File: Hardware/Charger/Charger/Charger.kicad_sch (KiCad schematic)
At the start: 0 parts

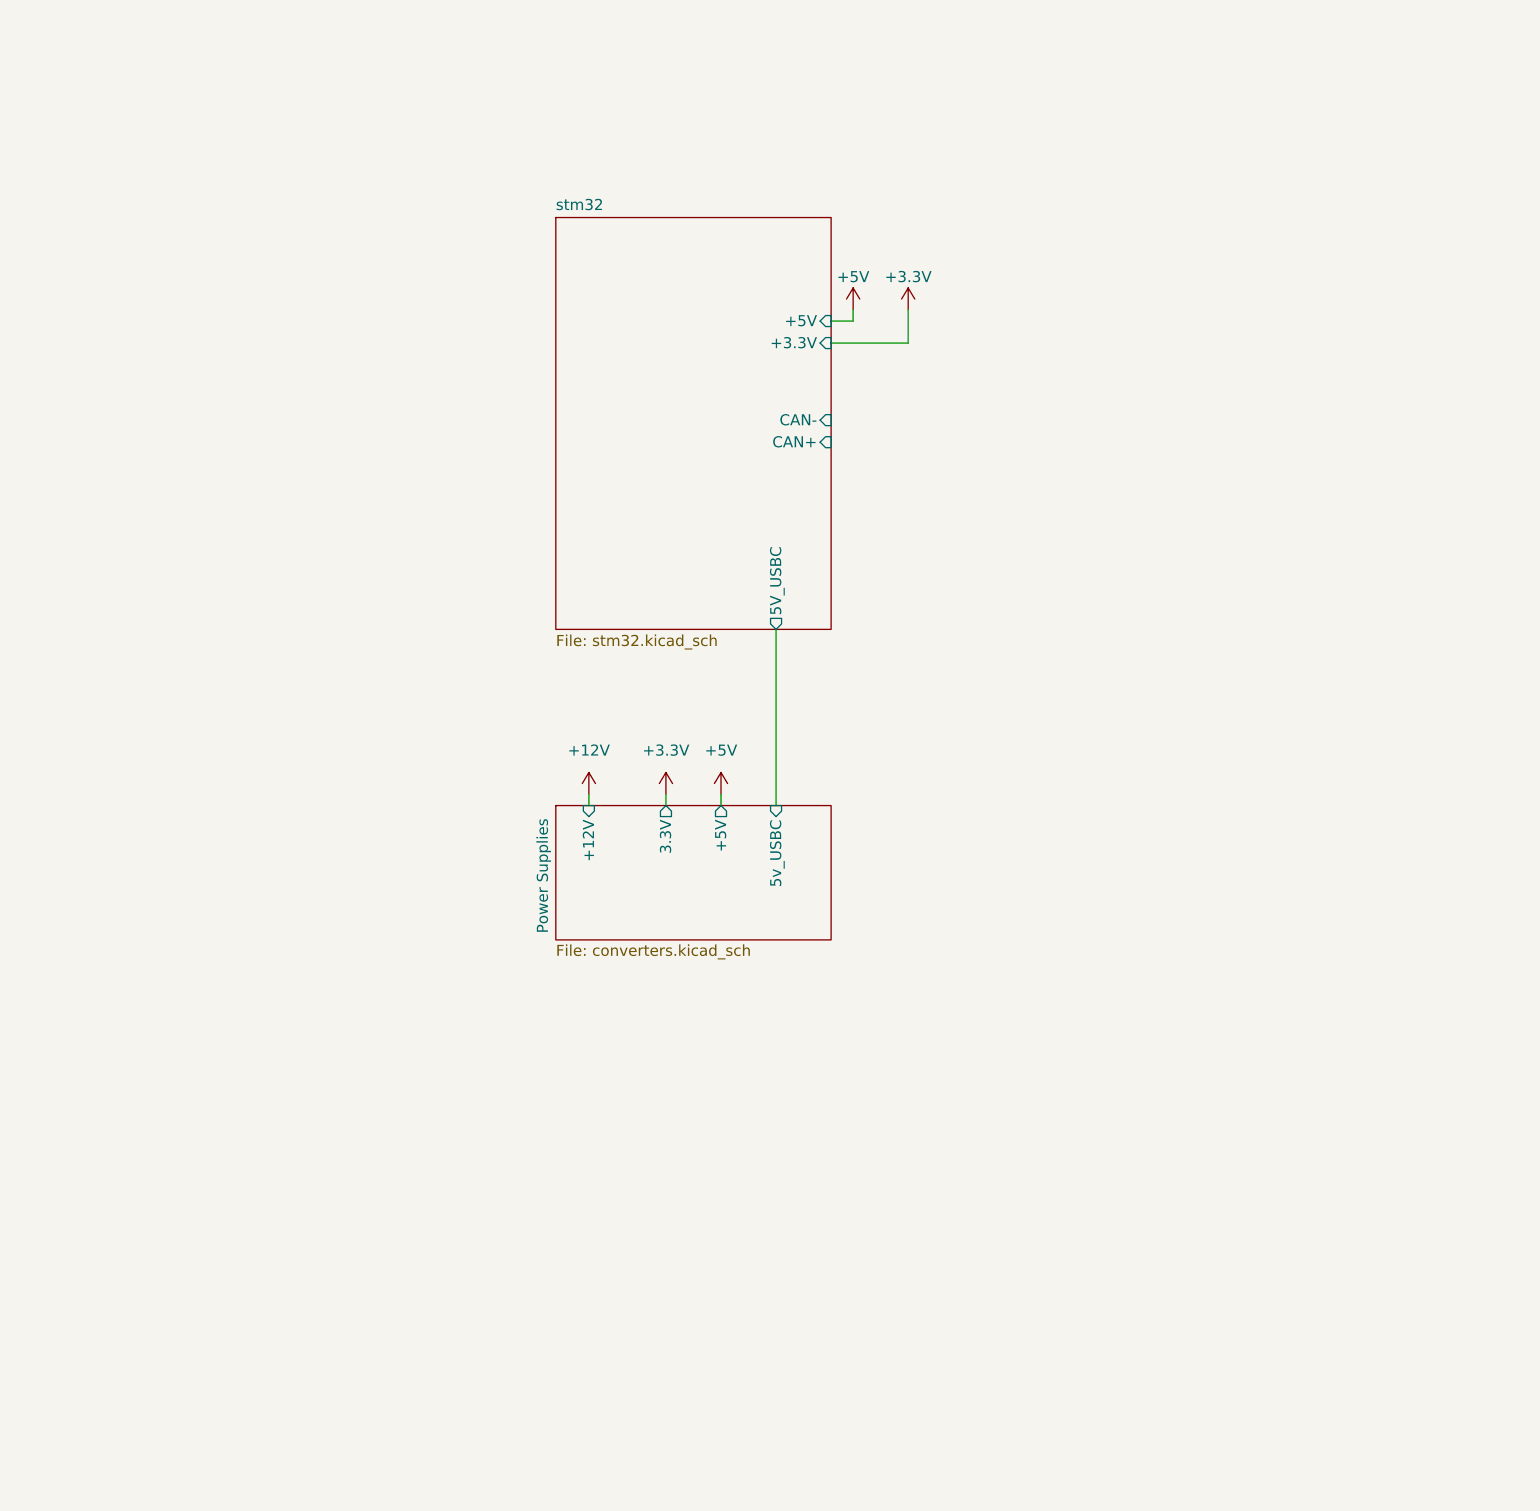
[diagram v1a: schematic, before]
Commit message: Added: Contactor control, Voltage sense, I2C comms for oled screen, 3v3 and 5v converters, power switch
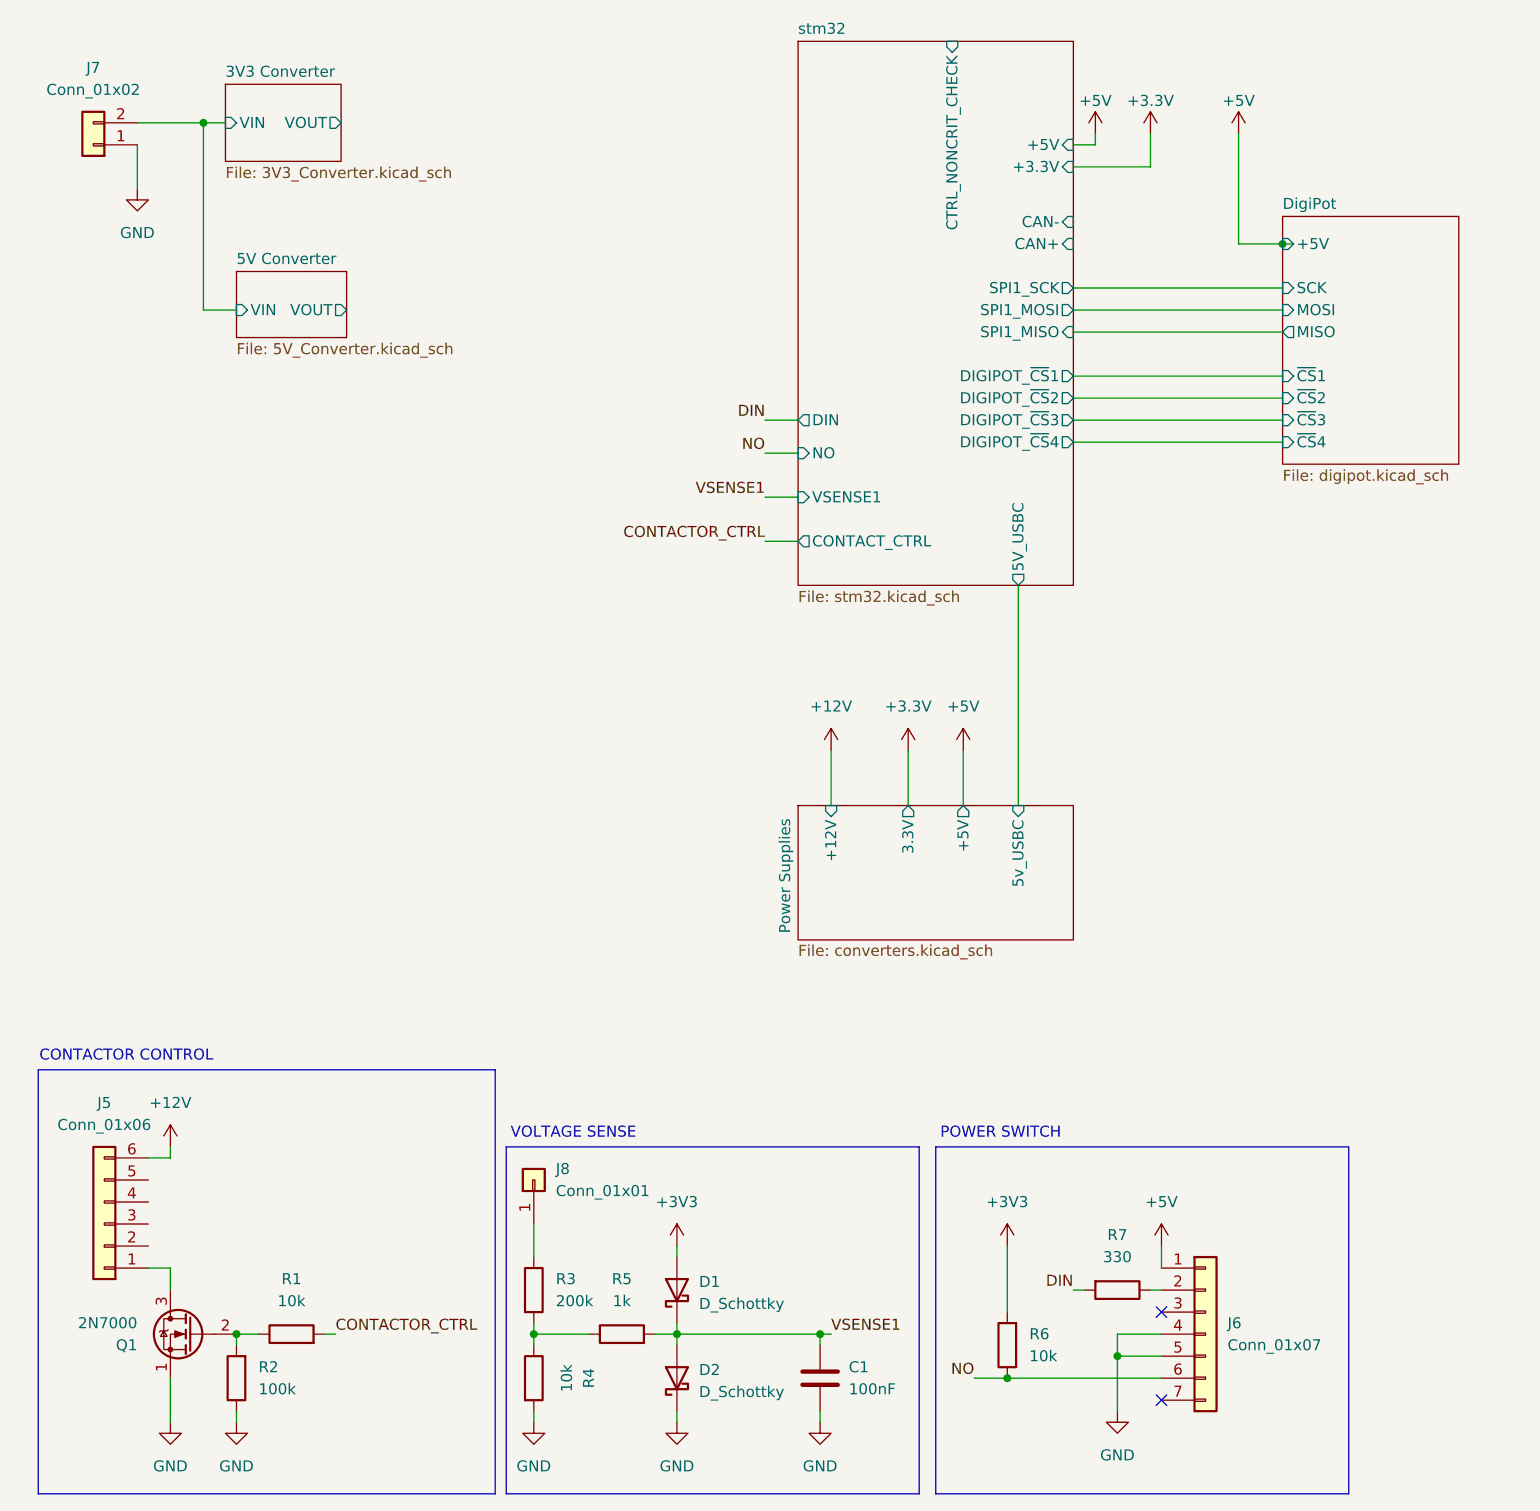
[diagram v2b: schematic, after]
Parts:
- added C1: 100nF, Capacitor_SMD:C_0603_1608Metric, symbol Device:C
- added D1, D2: D_Schottky, Diode_SMD:D_0201_0603Metric, symbol Device:D_Schottky
- added J5: Conn_01x06, Connector_Molex:Molex_Micro-Fit_3.0_43650-0600_1x06_P3.00mm_Horizontal, symbol Connector_Generic:Conn_01x06
- added J6: Conn_01x07, symbol Connector_Generic:Conn_01x07
- added J7: Conn_01x02, symbol Connector_Generic:Conn_01x02
- added J8: Conn_01x01, symbol Connector_Generic:Conn_01x01
- added Q1: 2N7000, Package_TO_SOT_THT:TO-92_Inline, symbol Transistor_FET:2N7000
- added R1, R4, R6: 10k, Resistor_SMD:R_0603_1608Metric, symbol Device:R
- added R2: 100k, Resistor_SMD:R_0603_1608Metric, symbol Device:R
- added R3: 200k, Resistor_SMD:R_0603_1608Metric, symbol Device:R
- added R5: 1k, Resistor_SMD:R_0603_1608Metric, symbol Device:R
- added R7: 330, Resistor_SMD:R_0603_1608Metric, symbol Device:R
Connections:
- net +12V: now also J5.6 (Pin_6)
- net +5V: now also J6.1 (Pin_1)
- new net: J8.1 (Pin_1), R3.1
- new net: R3.2, R4.1, R5.1
- new net: Q1.2 (G), R1.1, R2.2
- new net: J5.1 (Pin_1), Q1.3 (D)
- new net: J6.2 (Pin_2), R7.1
- new net +3V3: D1.2 (A), R6.2
- new net 3V3 Converter/VIN: J7.2 (Pin_2)
- new net CONTACTOR_CTRL: R1.2
- new net DIN: R7.2
- new net GND: C1.2, D2.1 (K), J6.4 (Pin_4), J6.5 (Pin_5), J7.1 (Pin_1), Q1.1 (S), R2.1, R4.2
- new net NO: J6.6 (Pin_6), R6.1
- new net VSENSE1: C1.1, D1.1 (K), D2.2 (A), R5.2
- no-connect marks 0 -> 2
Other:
- added sheet 3V3 Converter (3V3_Converter.kicad_sch)
- added sheet 5V Converter (5V_Converter.kicad_sch)
- added sheet DigiPot (digipot.kicad_sch)
- sheet stm32 ports: added CONTACT_CTRL, CTRL_NONCRIT_CHECK, DIGIPOT_~{CS}1, DIGIPOT_~{CS}2, DIGIPOT_~{CS}3, DIGIPOT_~{CS}4, DIN, NO, SPI1_MISO, SPI1_MOSI, SPI1_SCK, VSENSE1; removed none
- note added: "CONTACTOR CONTROL"
- note added: "POWER SWITCH"
- note added: "VOLTAGE SENSE"

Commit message: Few updates to connectors
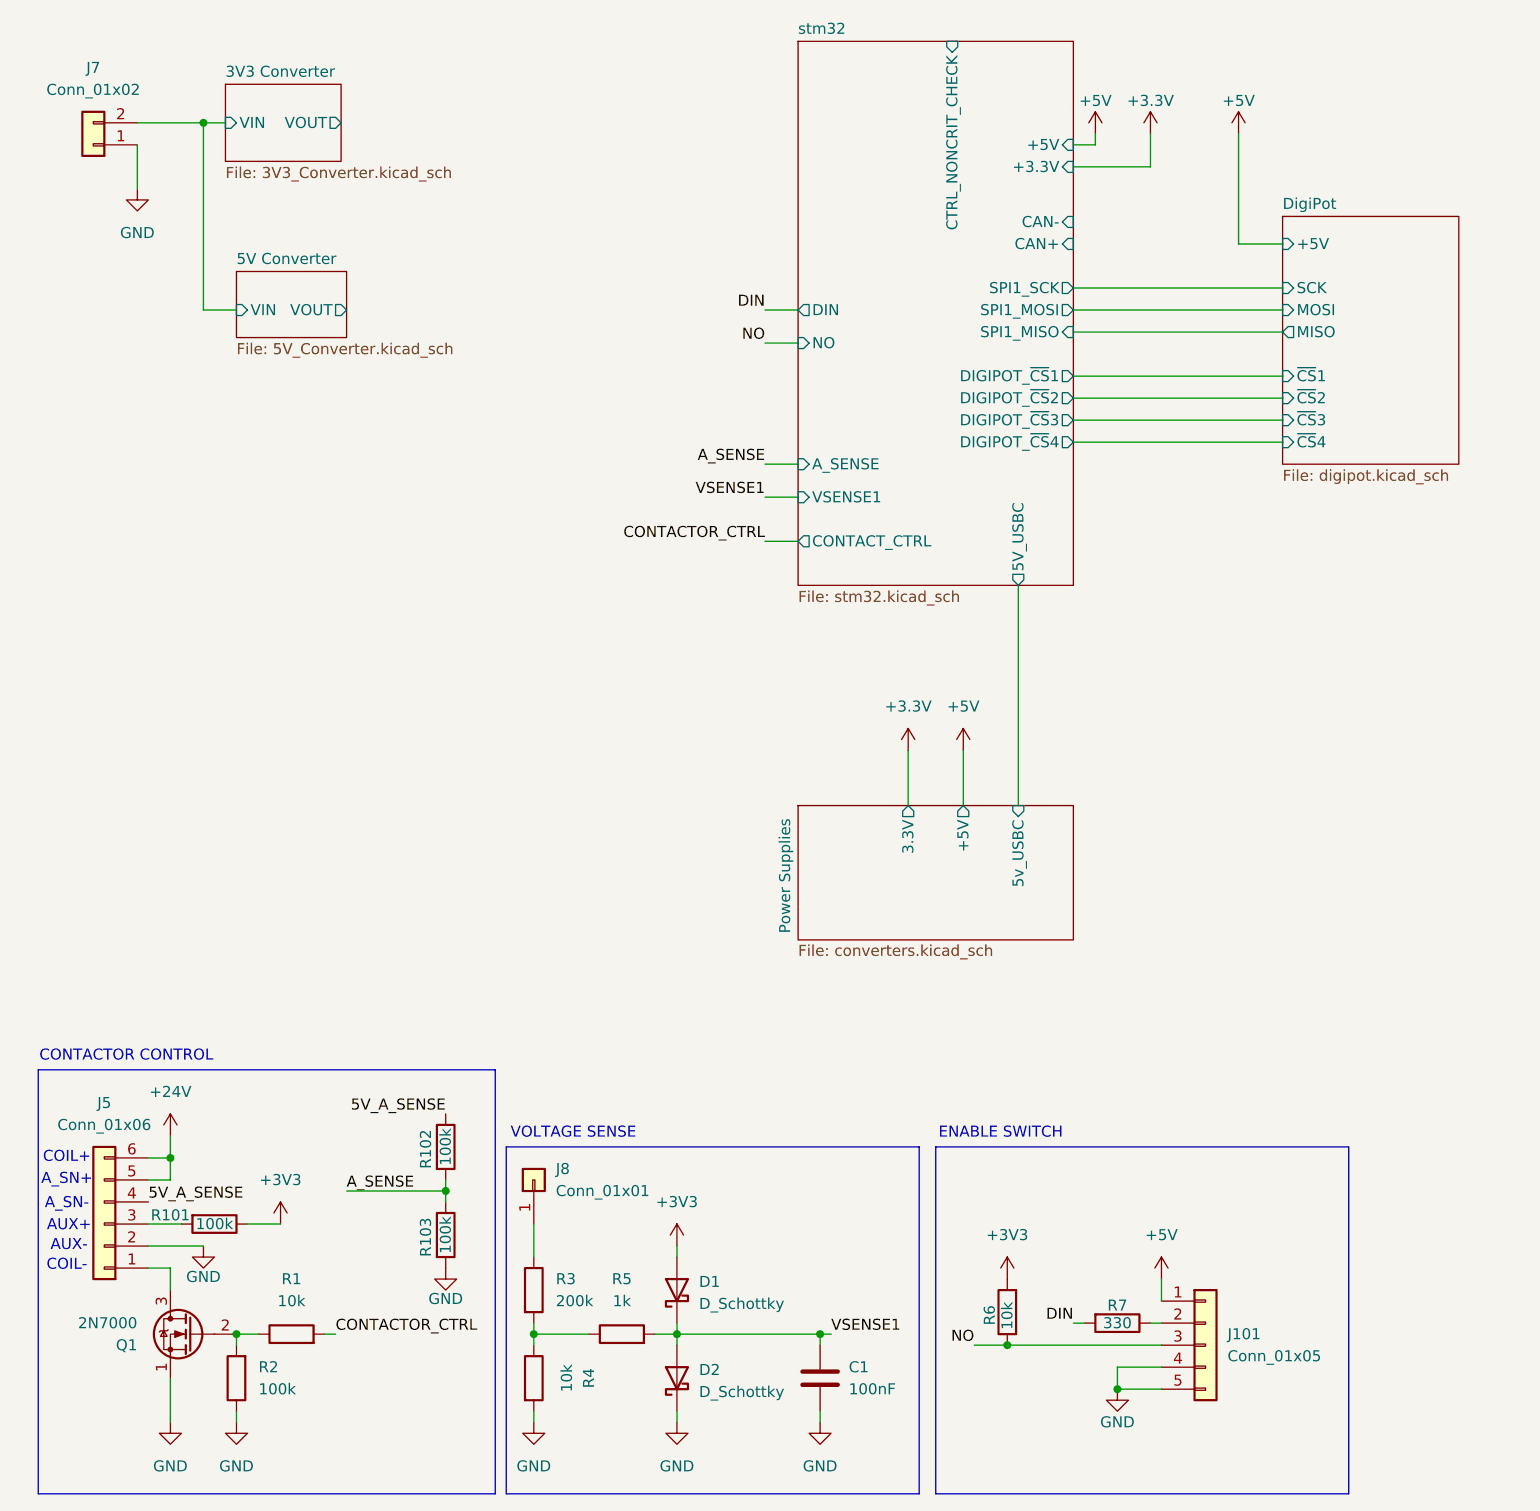
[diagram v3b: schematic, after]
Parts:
- removed J6: Conn_01x07, symbol Connector_Generic:Conn_01x07
- added J101: Conn_01x05, Connector_Molex:Molex_Micro-Fit_3.0_43650-0500_1x05_P3.00mm_Horizontal, symbol Connector_Generic:Conn_01x05
- added R101, R102, R103: 100k, Resistor_SMD:R_0603_1608Metric, symbol Device:R
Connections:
- net +12V is gone; now on net +24V: J5.6 (Pin_6)
- net +3V3: now also R101.1
- net +5V: now also J101.1 (Pin_1)
- net GND: now also J5.2 (Pin_2), J101.4 (Pin_4), J101.5 (Pin_5), R103.2
- net NO: now also J101.3 (Pin_3)
- net at R7.1: now also J101.2 (Pin_2)
- net at J5.3 (Pin_3): now also R101.2
- net 5V_A_SENSE: now reaches J5.4 (Pin_4)
- net 5V_A_SENSE: now also R102.1
- net +24V: now reaches J5.5 (Pin_5)
- new net A_SENSE: R102.2, R103.1
- no-connect marks 2 -> 0
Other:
- sheet Power Supplies ports: added none; removed +12V
- sheet stm32 ports: added A_SENSE; removed none
- note added: "AUX+"
- note added: "AUX-"
- note added: "A_SN+"
- note added: "A_SN-"
- note added: "COIL+"
- note added: "COIL-"
- note added: "ENABLE SWITCH"
- note removed: "POWER SWITCH"
- moved on the sheet: R6, R7

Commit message: Completed PCB layout of charger
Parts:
- removed J7: Conn_01x02, symbol Connector_Generic:Conn_01x02
- removed J8: Conn_01x01, symbol Connector_Generic:Conn_01x01
- removed Q1: 2N7000, Package_TO_SOT_THT:TO-92_Inline, symbol Transistor_FET:2N7000
- added J2: Conn_01x02, Connector_Molex:Molex_Micro-Fit_3.0_43650-0200_1x02_P3.00mm_Horizontal, symbol Connector_Generic:Conn_01x02
- added Q401: DMN10H220L, Package_TO_SOT_SMD:SOT-23, symbol Transistor_FET:DMN10H220L
- renumbered J5 to J1, J101 to J3, R101 to R1, R7 to R10, R1 to R3, R102 to R4, R103 to R5, R3 to R6, R4 to R7, R5 to R8, R6 to R9
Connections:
- net +3.3V: now also D1.2 (A), R9.2
- net +3V3: no longer D1.2 (A), R9.2
- net GND: now also J2.2 (Pin_2), Q401.2 (S)
- net at R6.1: now also J2.1 (Pin_1)
- net at R2.2, R3.1: now also Q401.1 (G)
- net at J1.1 (Pin_1): now also Q401.3 (D)
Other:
- removed sheet 3V3 Converter
- removed sheet 5V Converter
- moved on the sheet: C1, D1, D2, R7, R8
